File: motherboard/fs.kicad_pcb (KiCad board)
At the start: 4 copper layers, 177.8 x 114.3 mm, 221 parts, among them J101 SC10L, J102 640389-2, J201 BNC, J202 Conn_01x05, J203 BNC, J301 BNC, J302 BNC, J303 BNC, J304 BNC, J305 BNC, J306 BNC, Q101 MJD44H11, Q102 MJD45H11, Q201 2N7002, Q202 2N7002, Q203 2N7002, U101 INA132UA, U102 LM741C, U103 LMH6609, U104 LM317, U105 LM337, U106 LM340-5, U107 MC7905ACD2T, U201 LMH6609, U202 SYPD-1, U203 LM393, U204 AD797AR, U205 LM393, U206 OPA192IDR, U301 LMH6609, U302 LMH6609, U303 LMH6609, U304 LMH6609, U305 LMH6609, U306 LMH6609

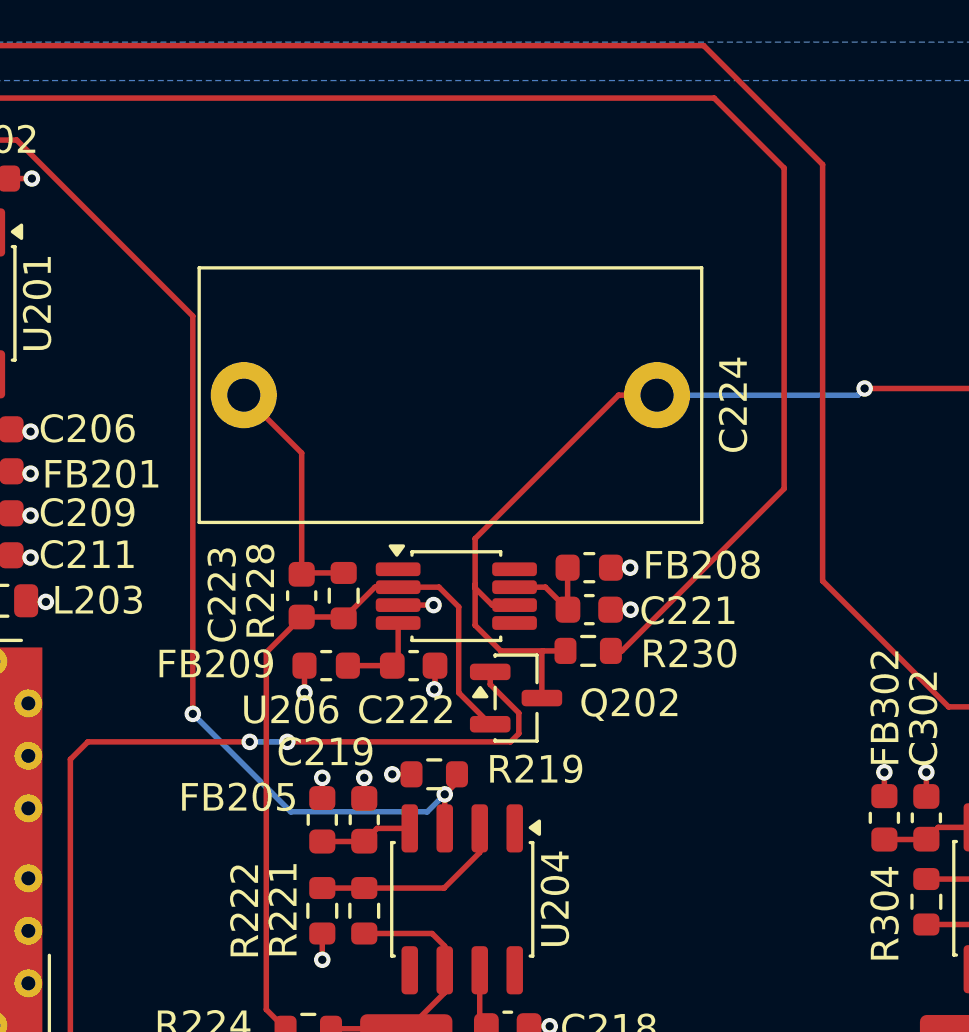
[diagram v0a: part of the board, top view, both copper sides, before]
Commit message: use SOIC-8 for OPA192IDR
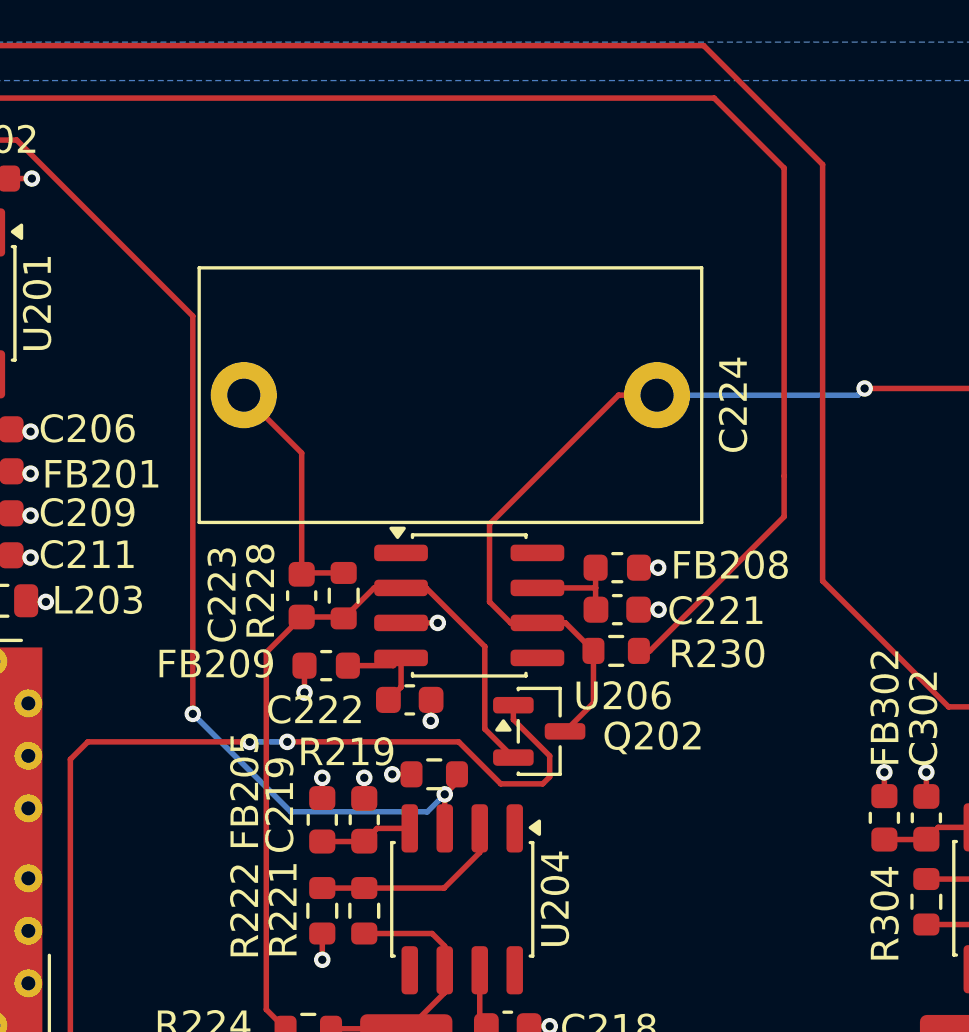
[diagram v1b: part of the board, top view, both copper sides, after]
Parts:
- U206: footprint Package_SO:VSSOP-8_3x3mm_P0.65mm -> Package_SO:SOIC-8_3.9x4.9mm_P1.27mm
- moved Q202 1.47 mm to (78.1, 118.9)
- moved C222 1.25 mm to (73.4, 117.7)
- moved C221 1.02 mm to (80.9, 114.5)
- moved FB208 1.02 mm to (80.9, 112.9)
- moved R230 1.02 mm to (80.9, 116.0)
- moved U206 0.58 mm to (75.6, 114.3)
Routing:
- net /Phase Noise/~{SIG_PRESENT}: track 149.2 -> 151.4 mm
- net Net-(Q202-S): track 27.1 -> 28.3 mm
- net Net-(U206-V–): track 3.25 -> 3.76 mm

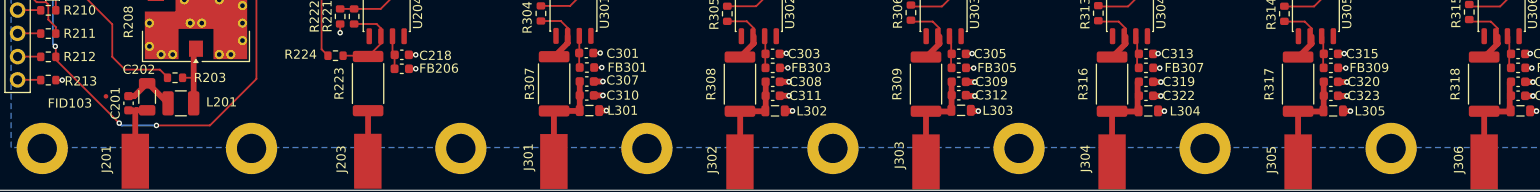
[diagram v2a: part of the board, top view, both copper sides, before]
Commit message: add ESD protection (14V TVS)
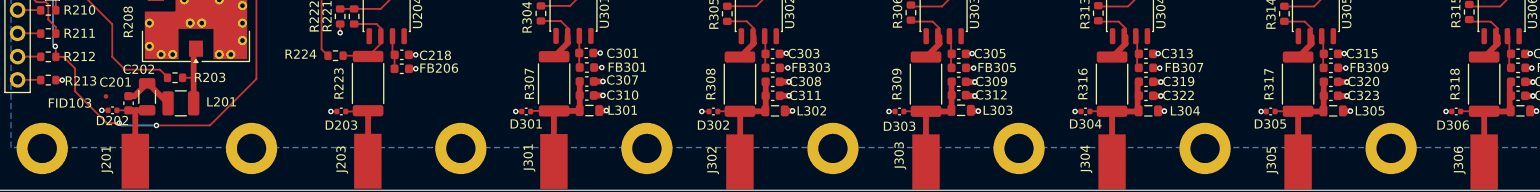
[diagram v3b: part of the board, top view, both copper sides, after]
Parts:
- added D202: 14V TVS, Capacitor_SMD:C_0402_1005Metric, F.Cu at (45.4, 135.6)
- added D203: 14V TVS, Capacitor_SMD:C_0402_1005Metric, F.Cu at (70.4, 135.8)
- added D301: 14V TVS, Capacitor_SMD:C_0402_1005Metric, F.Cu at (90.6, 135.8)
- added D302: 14V TVS, Capacitor_SMD:C_0402_1005Metric, F.Cu at (111.0, 135.8)
- added D303: 14V TVS, Capacitor_SMD:C_0402_1005Metric, F.Cu at (131.3, 135.8)
- added D304: 14V TVS, Capacitor_SMD:C_0402_1005Metric, F.Cu at (151.6, 135.8)
- added D305: 14V TVS, Capacitor_SMD:C_0402_1005Metric, F.Cu at (171.9, 135.8)
- added D306: 14V TVS, Capacitor_SMD:C_0402_1005Metric, F.Cu at (192.1, 135.8)
- C103, C204, C212, C214, C223: value 1nF -> 1nF NP0
- L203, L301, L302, L303, L304, L305, L306: value 1.5UH -> 1.5μH
- R104: value 61.9 -> 61.9R
- R109: value 162 -> 162R
- R216: value 130 -> 130R
- R221: value 374 -> 374R
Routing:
- net GND: track 95.3 -> 100.6 mm, vias 101 -> 109
- net /Outputs/OUT1: track 11.5 -> 14.1 mm
- net /Outputs/OUT6: track 11.5 -> 14.1 mm
- net /Outputs/OUT5: track 11.5 -> 14.0 mm
- net Net-(D203-CATHODE): track 5.53 -> 8.01 mm
- net /Outputs/OUT3: track 11.5 -> 13.9 mm
- net /Outputs/OUT2: track 11.5 -> 13.9 mm
- net /Outputs/OUT4: track 11.5 -> 13.9 mm
- net /Phase Noise/~{SIG_PRESENT}: track 151.4 -> 152.7 mm
- net Net-(D202-CATHODE): track 7.66 -> 8.93 mm

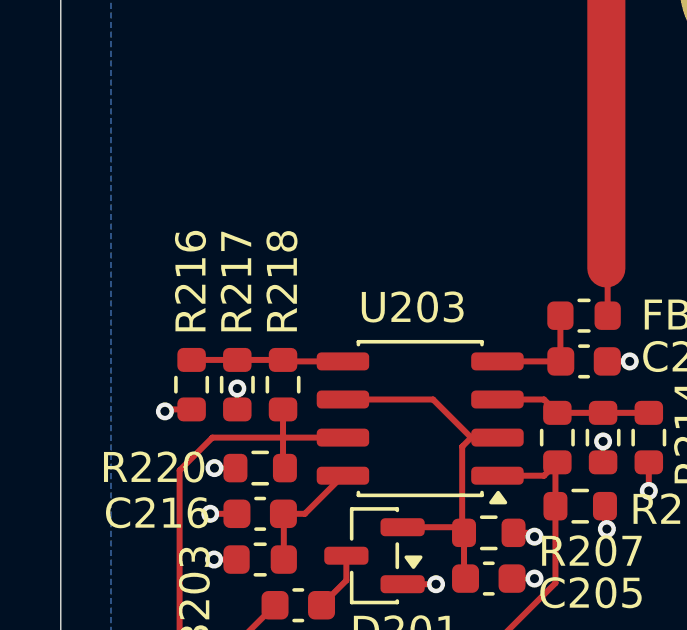
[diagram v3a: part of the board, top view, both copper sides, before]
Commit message: retune comparator thresholds for 1--3 Vpp
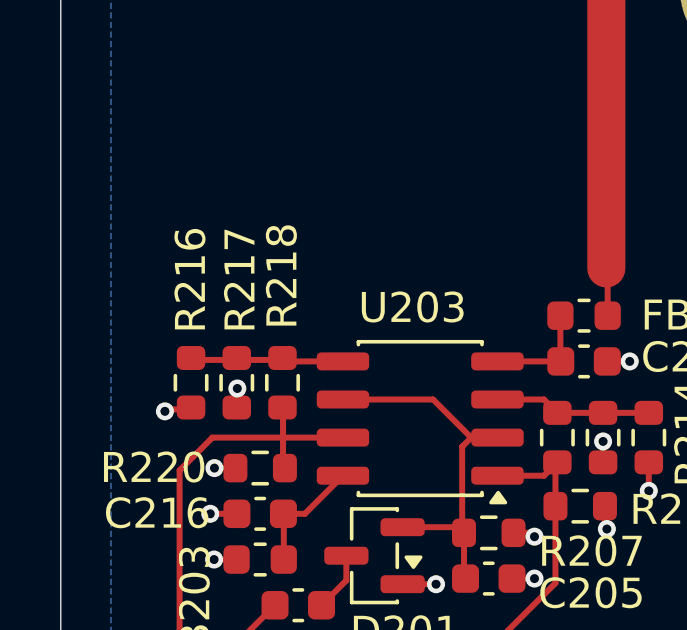
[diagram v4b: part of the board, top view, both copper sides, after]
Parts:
- removed the R216 at (37.0, 55.2)
- added R218: 1.00M, Resistor_SMD:R_0603_1608Metric, F.Cu at (40.0, 55.1)
- J101: value SC10L -> Header
- R217: value 100R -> 10.0K
- moved R216 3.07 mm to (37.0, 55.1)
- moved R217 0.07 mm to (38.5, 55.1), turned to 90 degrees
- renumbered R218 to R216
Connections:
- R216 pad 1: /Phase Noise/3.9V -> /Phase Noise/2.3V
- R216 pad 2: /Phase Noise/~{OVLD} -> +9V
- R217 pad 1: /Phase Noise/3.9V -> GND
- R217 pad 2: GND -> /Phase Noise/2.3V
- U203 pad 5: /Phase Noise/3.9V -> /Phase Noise/2.3V
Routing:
- net /Phase Noise/3.9V: track 4.60 -> 0.00 mm
- net /Phase Noise/2.3V: track 0.00 -> 4.60 mm

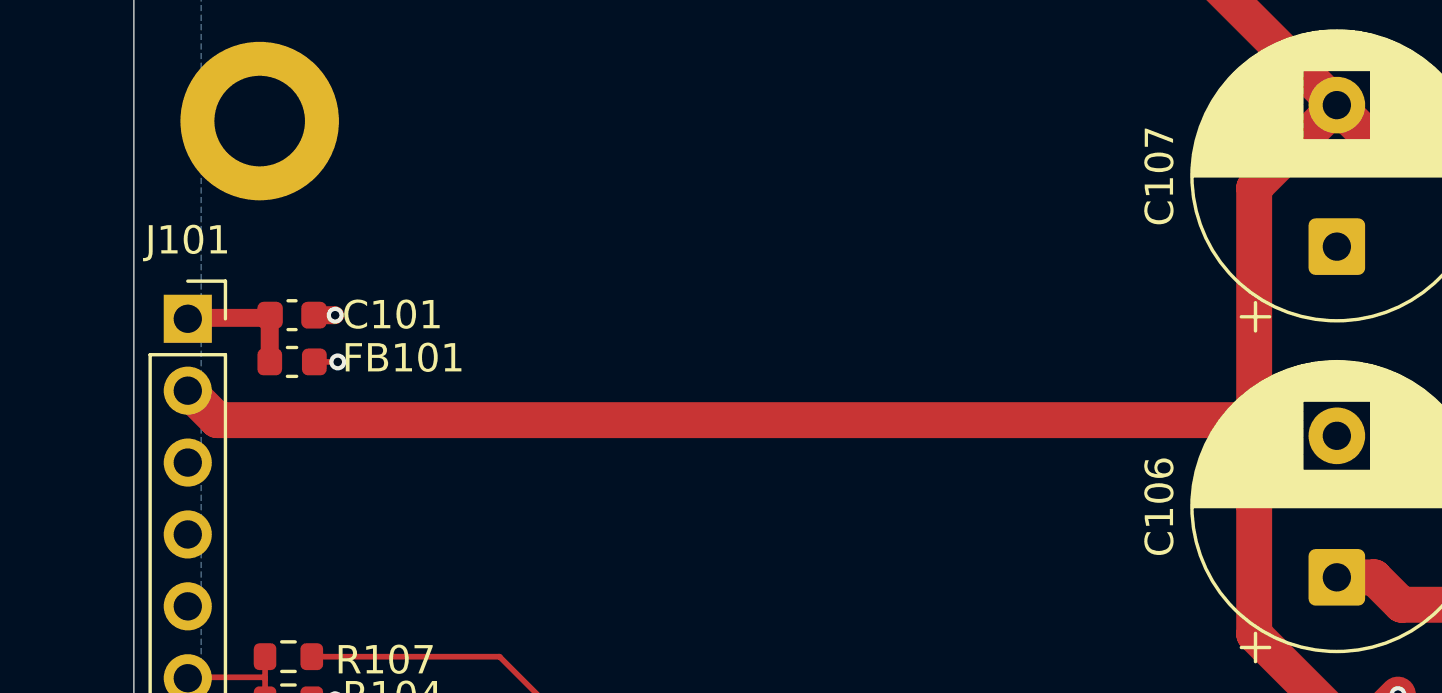
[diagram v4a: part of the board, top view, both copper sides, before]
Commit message: update OCXO bead to SMB2.5R-2 (higher current)
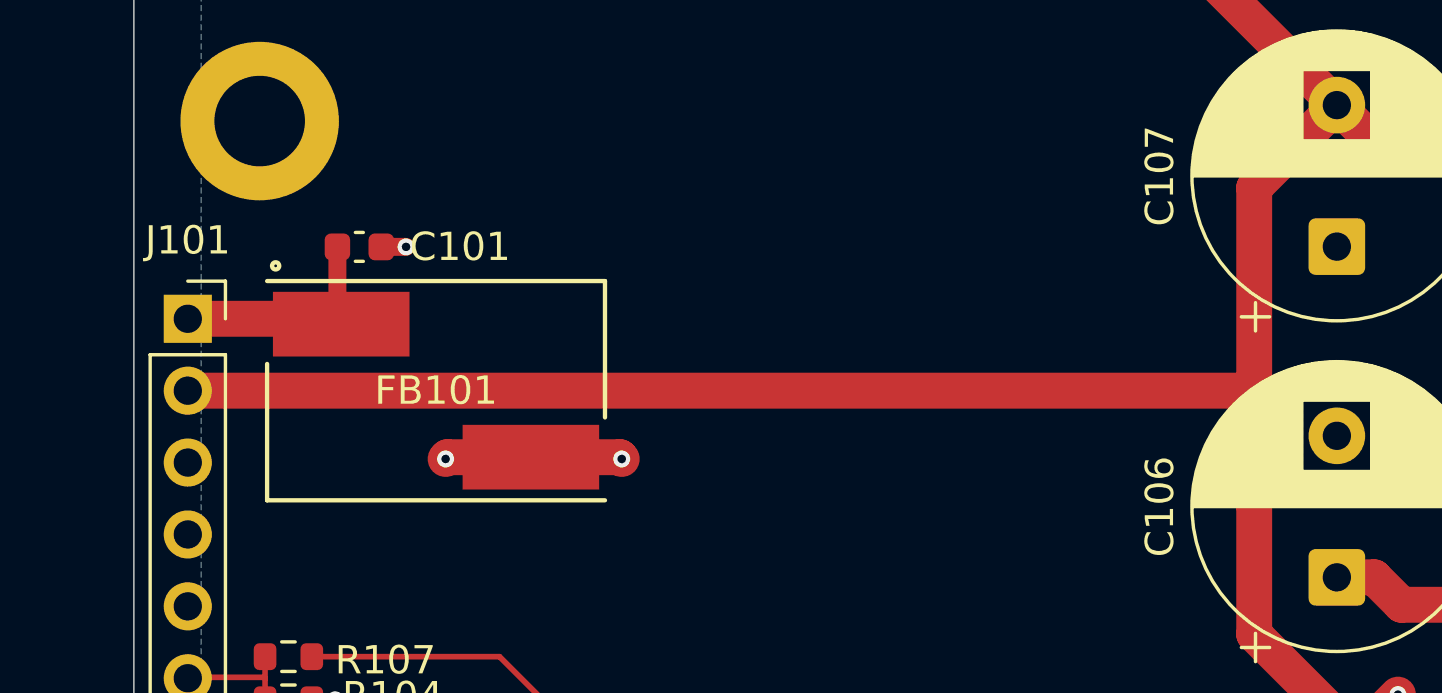
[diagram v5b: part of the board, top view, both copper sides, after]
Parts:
- FB101: footprint Inductor_SMD:L_0603_1608Metric -> INDUCTOR_SRS:SMB2.5R-2
- moved FB101 5.19 mm to (123.2, 51.4)
- moved C101 3.39 mm to (120.5, 46.4)
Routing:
- net +12V: track 48.5 -> 54.0 mm, vias 7 -> 8
- net /B+24V: track 4.54 -> 8.29 mm

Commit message: add fab notes
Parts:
- moved C114 5.14 mm to (177.5, 81.2), turned to -90 degrees
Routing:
- net +9V: track 27.7 -> 9.46 mm, vias 13 -> 20
- added copper zone on F.Cu, net +9V
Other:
- board text added: "FABRICATION NOTES 1. BOARD IS NOT IMPEDANCE CONTROLLED. 2. OVERALL THICKNESS IS 1.6 mm. MATERIAL IS FR4 TG155. 3. ANY STACKUP ACCEPTABLE. 4. SURFACE FINISH IS ENIG. GOLD THICKNESS 2 μin = 0.05 μm. 5. VIAS SHOULD BE EPOXY FILLED & CAPPED."
